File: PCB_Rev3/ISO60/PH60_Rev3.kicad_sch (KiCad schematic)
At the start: 27 parts, among them J2 Conn_01x02, J3 Conn_01x04, U1 NCP1117-3.3_SOT223, U2 W25Q128JVS, U3 RP2040, Y1 Crystal_GND24

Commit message: Update PCB Rev3
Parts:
- removed J3: Conn_01x04, Connector_FFC-FPC:Molex_200528-0040_1x04-1MP_P1.00mm_Horizontal, symbol Connector_Generic:Conn_01x04
- removed R2: DNF, Resistor_SMD:R_0402_1005Metric, symbol Device:R
- added J1: USB_C_Receptacle_USB2.0_16P, Connector_USB:USB_C_Receptacle_GCT_USB4105-xx-A_16P_TopMnt_Horizontal, symbol Connector:USB_C_Receptacle_USB2.0_16P
- added R6, R7: 5K1, Resistor_SMD:R_0402_1005Metric, symbol Device:R
- C2, C3: value 15p -> 20p
- U1: value NCP1117-3.3_SOT223 -> TLV1117-33; symbol Regulator_Linear:NCP1117-3.3_SOT223 -> Regulator_Linear:TLV1117-33
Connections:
- net GND: now also J1.A1 (GND), J1.A12 (GND), J1.B1 (GND), J1.B12 (GND), R6.2, R7.2
- net USB_D+: now also J1.A6 (D+), J1.B6 (D+)
- net USB_D-: now also J1.A7 (D-), J1.B7 (D-)
- net VBUS: now also J1.A4 (VBUS), J1.A9 (VBUS), J1.B4 (VBUS), J1.B9 (VBUS)
- new net: J1.B5 (CC2), R7.1
- new net: J1.A5 (CC1), R6.1
- no-connect marks 13 -> 16
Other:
- moved on the sheet: C1, C4, U1

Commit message: modify routing
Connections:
- net RUN: no longer names the net of U3.26 (RUN)
- no-connect marks 16 -> 17
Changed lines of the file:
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@@
+	)
+	(no_connect
+		(at 83.82 73.66)
 	)
 	(no_connect
@@
 		(pts
 			(xy 119.38 41.91) (xy 119.38 33.02)
-		)
-		(stroke
-			(width 0)
-			(type default)
-		)
-	)
-	(wire
-		(pts
-			(xy 67.31 73.66) (xy 83.82 73.66)
 		)
 		(stroke
@@
 		(fields_autoplaced yes)
 		(effects
-			(font
-				(size 1.27 1.27)
-			)
-			(justify left bottom)
-		)
-	)
-	(label "RUN"
-		(at 67.31 73.66 0)
-		(fields_autoplaced yes)
-		(effects

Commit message: PCB Rev3 Layout
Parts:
- J2: footprint Connector_PinHeader_1.00mm:PinHeader_1x02_P1.00mm_Vertical -> Connector_PinHeader_2.54mm:PinHeader_1x02_P2.54mm_Vertical
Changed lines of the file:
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@@
 			)
 		)
-		(property "Footprint" "Connector_PinHeader_1.00mm:PinHeader_1x02_P1.00mm_Vertical"
+		(property "Footprint" "Connector_PinHeader_2.54mm:PinHeader_1x02_P2.54mm_Vertical"
 			(at 191.77 109.22 0)
 			(effects

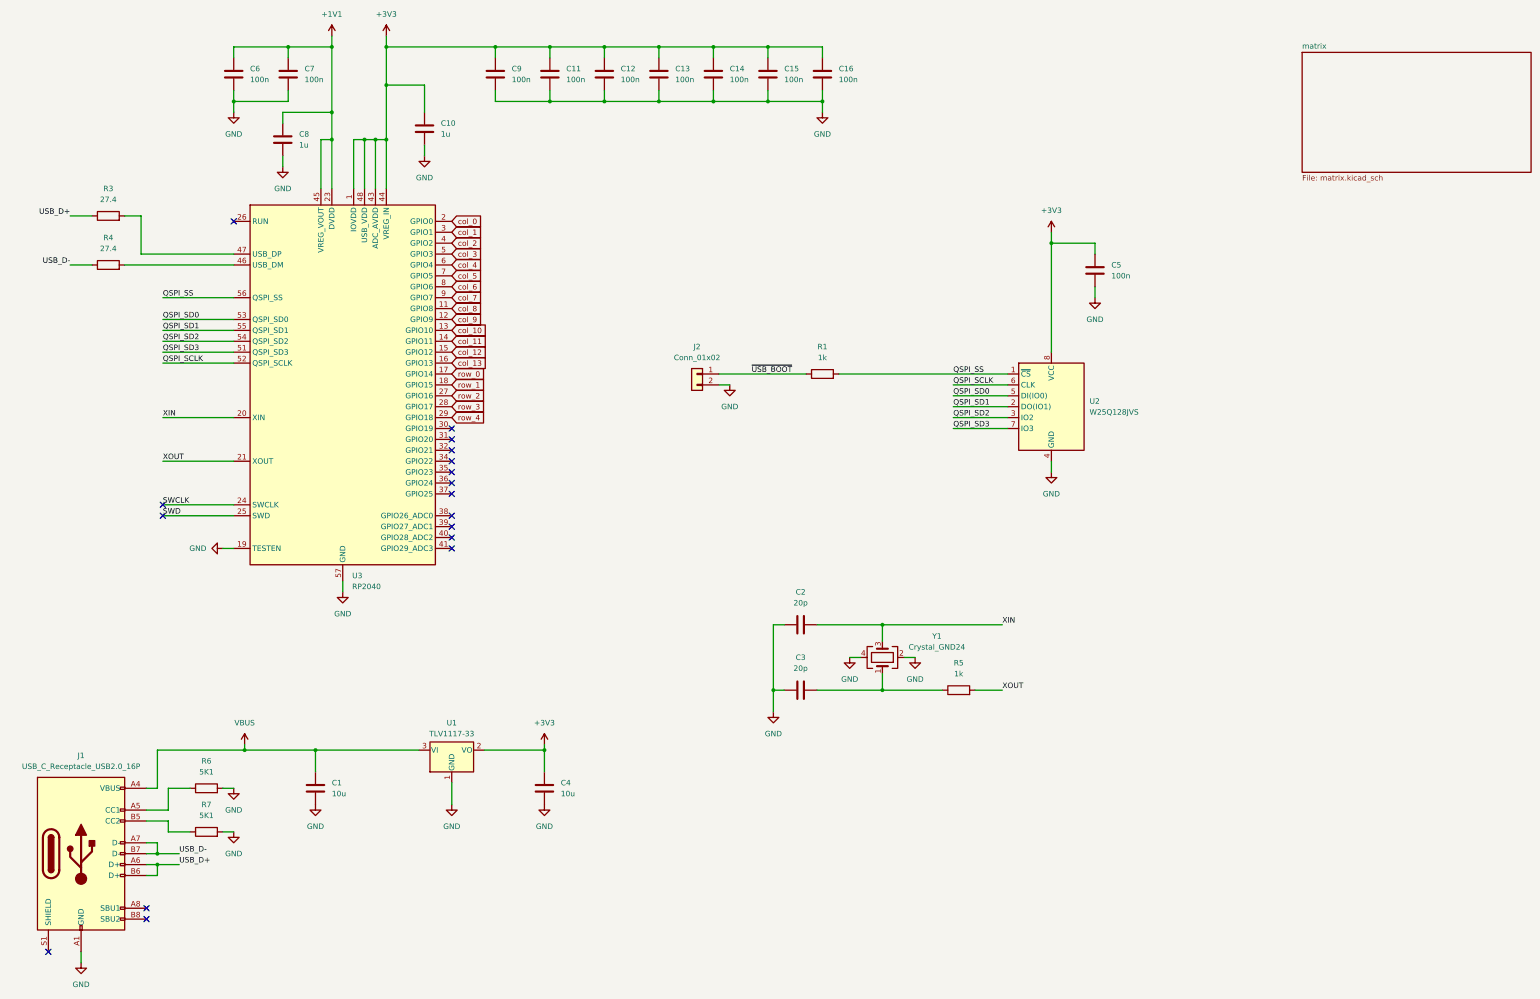
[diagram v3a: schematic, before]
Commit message: Add RGB Lighting for PCB Rev3
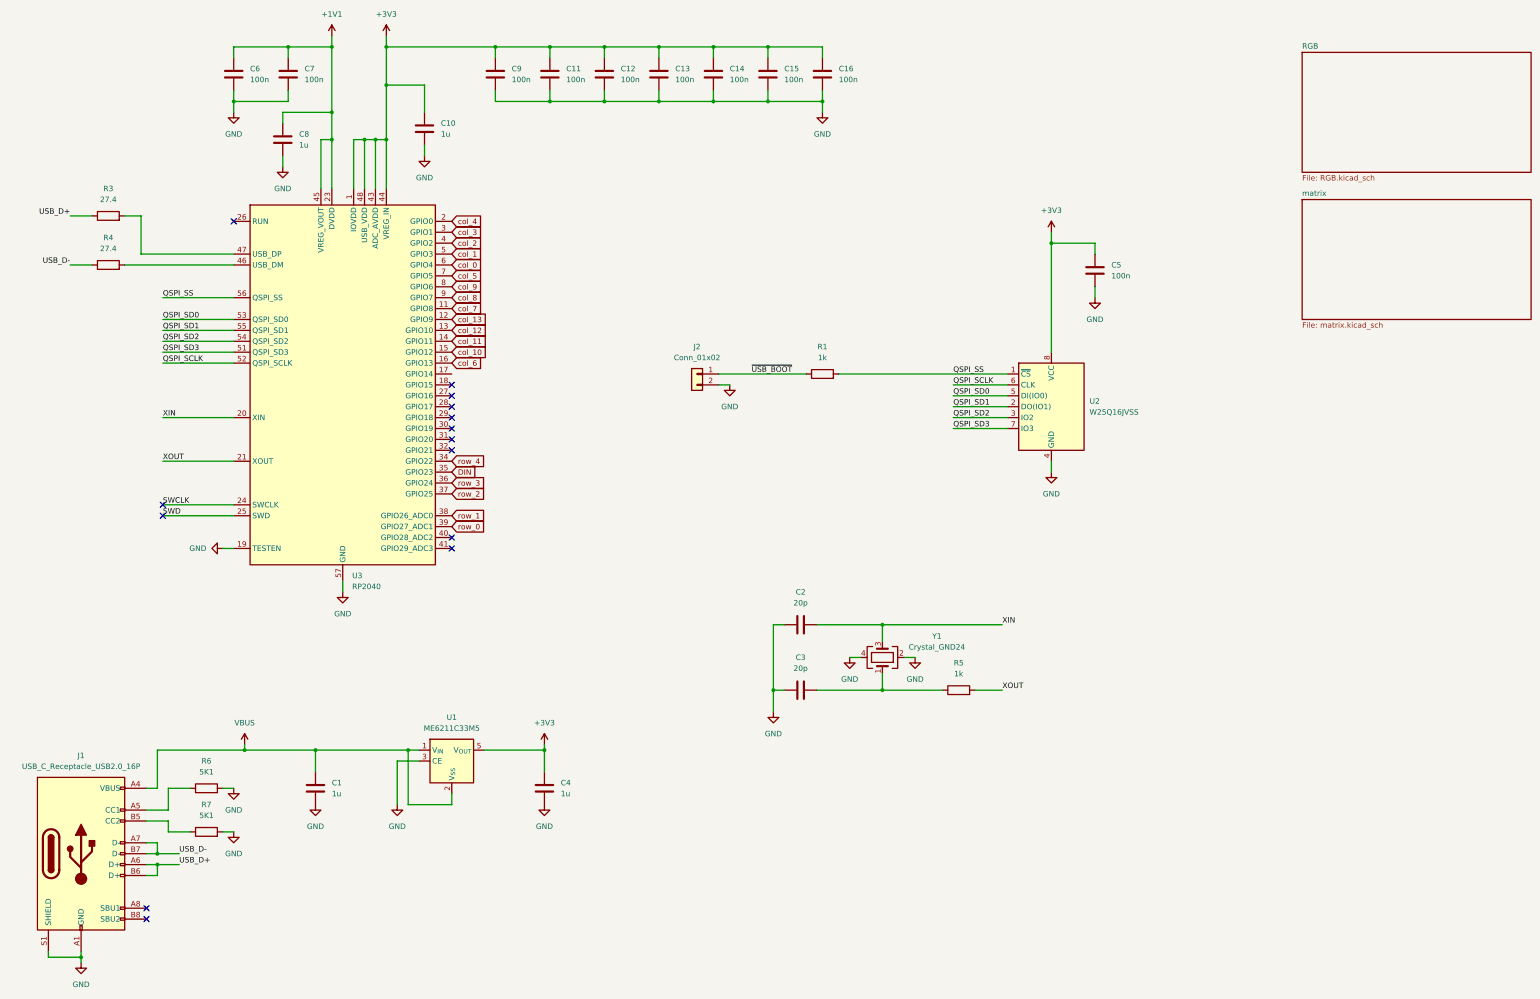
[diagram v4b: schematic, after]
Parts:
- removed U1: TLV1117-33, Package_TO_SOT_SMD:SOT-223, symbol Regulator_Linear:TLV1117-33
- removed U2: W25Q128JVS, Package_SO:SOIC-8_5.23x5.23mm_P1.27mm, symbol Memory_Flash:W25Q128JVS
- added U1: ME6211C33M5, Package_TO_SOT_SMD:SOT-23-5, symbol Regulator_Linear:ME6211C33M5
- added U2: W25Q16JVSS, Package_SON:Winbond_USON-8-1EP_3x2mm_P0.5mm_EP0.2x1.6mm, symbol Memory_Flash:W25Q16JVSS
- C1, C4: value 10u -> 1u
- U3: footprint Package_DFN_QFN:QFN-56-1EP_7x7mm_P0.4mm_EP3.2x3.2mm -> Package_DFN_QFN:QFN-56-1EP_7x7mm_P0.4mm_EP3.2x3.2mm_ThermalVias
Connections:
- net +3V3: now also U1.5 (V_{OUT}), U2.8 (VCC)
- net GND: now also J1.S1 (SHIELD), U1.3 (CE), U2.4 (GND)
- net QSPI_SCLK: now also U2.6 (CLK)
- net QSPI_SD0: now also U2.5 (DI(IO0))
- net QSPI_SD1: now also U2.2 (DO(IO1))
- net QSPI_SD2: now also U2.3 (IO2)
- net QSPI_SD3: now also U2.7 (IO3)
- net QSPI_SS: now also U2.1 (~{CS})
- net VBUS: now also U1.1 (V_{IN}), U1.2 (V_{SS})
- net col_0: now also U3.6 (GPIO4); no longer U3.2 (GPIO0)
- net col_1: now also U3.5 (GPIO3); no longer U3.3 (GPIO1)
- net col_10: now also U3.15 (GPIO12); no longer U3.13 (GPIO10)
- net col_12: now also U3.13 (GPIO10); no longer U3.15 (GPIO12)
- net col_13: now also U3.12 (GPIO9); no longer U3.16 (GPIO13)
- net col_3: now also U3.3 (GPIO1); no longer U3.5 (GPIO3)
- net col_4: now also U3.2 (GPIO0); no longer U3.6 (GPIO4)
- net col_6: now also U3.16 (GPIO13); no longer U3.8 (GPIO6)
- net col_7: now also U3.11 (GPIO8); no longer U3.9 (GPIO7)
- net col_8: now also U3.9 (GPIO7); no longer U3.11 (GPIO8)
- net col_9: now also U3.8 (GPIO6); no longer U3.12 (GPIO9)
- net row_0: now also U3.39 (GPIO27_ADC1); no longer U3.17 (GPIO14)
- net row_1: now also U3.38 (GPIO26_ADC0); no longer U3.18 (GPIO15)
- net row_2: now also U3.37 (GPIO25); no longer U3.27 (GPIO16)
- net row_3: now also U3.36 (GPIO24); no longer U3.28 (GPIO17)
- net row_4: now also U3.34 (GPIO22); no longer U3.29 (GPIO18)
- net DIN: now reaches U3.35 (GPIO23)
- no-connect marks 17 -> 14
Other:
- added sheet RGB (RGB.kicad_sch)
